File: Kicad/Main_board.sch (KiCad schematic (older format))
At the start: 138 parts, among them J1 Data, J2 Power, J3 Data, SW1 SW_Push, SW10 SW_Push, SW11 SW_Push, SW12 SW_Push, SW13 SW_Push, SW14 SW_Push, SW15 SW_Push, SW16 SW_Push, SW17 SW_Push, SW18 SW_Push, SW19 SW_Push, SW2 SW_Push, SW20 SW_Push, SW21 Rotary_Encoder_Switch, SW22 Rotary_Encoder_Switch, SW23 Rotary_Encoder_Switch, SW24 SW_Rotary8, SW3 SW_Push, SW4 SW_Push, SW5 SW_Push, SW6 SW_Push, SW7 SW_Push, SW8 SW_Push, SW9 SW_Push, U1 74HC595, U2 74HC595, U3 74HC595, U4 74HC595, U5 7_segment_3_digit_2831AS

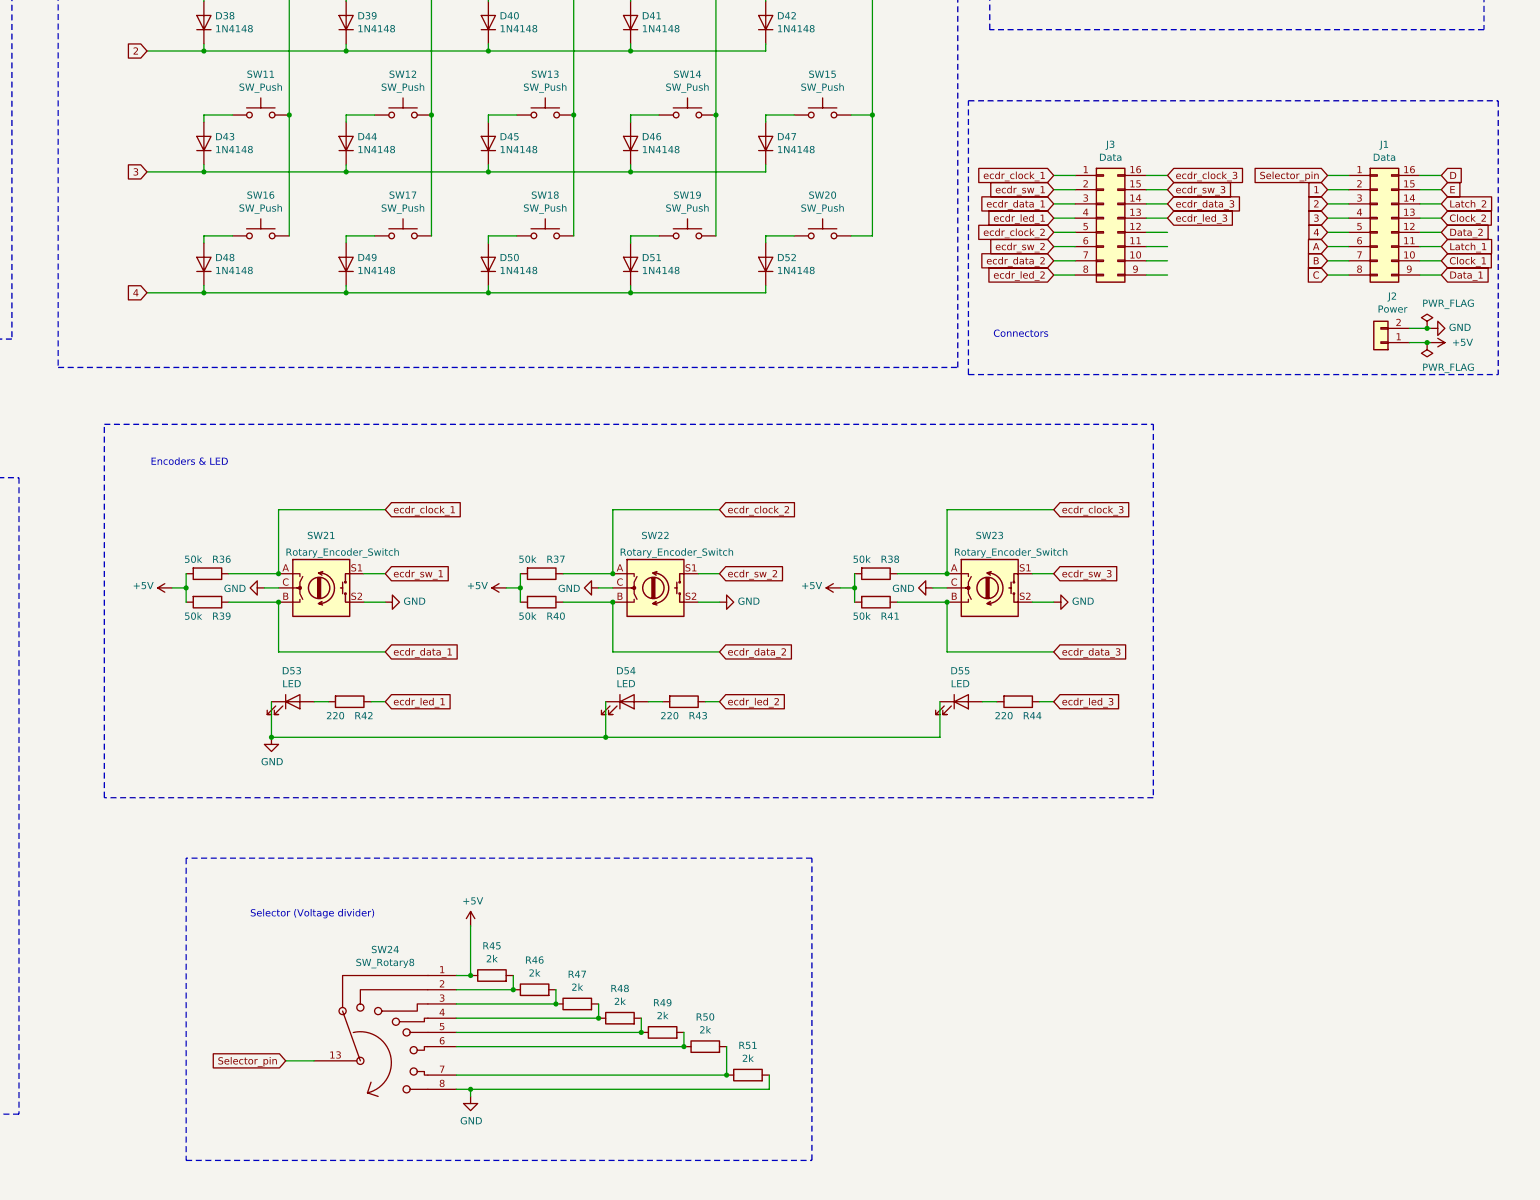
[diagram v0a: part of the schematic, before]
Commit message: modifié :         Kicad/Main_board-cache.lib 	modifié :         Kicad/Main_board.kicad_pcb 	modifié :         Kicad/Main_board.net 	modifié :         Kicad/Main_board.sch 	nouveau fichier : Kicad/My_library/00_Mes_empreintes.pretty/7-Segment_2831AS.kicad_mod 	modifié :         Kicad/My_library/00_Mes_empreintes.pretty/DIP-16_Socket.kicad_mod 	nouveau fichier : Kicad/My_library/00_Mes_empreintes.pretty/IDC-Header_2x04.kicad_mod 	nouveau fichier : Kicad/My_library/00_Mes_empreintes.pretty/IDC-Header_2x05.kicad_mod 	modifié :         Kicad/My_library/00_Mes_empreintes.pretty/IDC-Header_2x08.kicad_mod 	modifié :         Kicad/My_library/00_Mes_empreintes.pretty/LED_5.0mm.kicad_mod 	nouveau fichier : Kicad/My_library/00_Mes_empreintes.pretty/RotaryEncoder.kicad_mod 	modifié :         Kicad/My_library/00_Mes_empreintes.pretty/SW_PUSH-12mm(deported).kicad_mod 	modifié :         Kicad/My_library/00_Mes_symboles.bck 	modifié :         Kicad/My_library/00_Mes_symboles.dcm 	modifié :         Kicad/My_library/00_Mes_symboles.lib 	nouveau fichier : Kicad/My_library/Encoders.lib 	nouveau fichier : "Kicad/My_library/Mes_mod\303\250les_3D/216-resistors-in-tht-series-e24-from-1ohm-to-910mohm-1.snapshot.3/Yageo CFR-25 Resistor Axial P7.62mm 1,0 MOhm.stp" 	nouveau fichier : "Kicad/My_library/Mes_mod\303\250les_3D/216-resistors-in-tht-series-e24-from-1ohm-to-910mohm-1.snapshot.3/Yageo CFR-25 Resistor Axial P7.62mm 1,0 Ohm.stp" 	nouveau fichier : "Kicad/My_library/Mes_mod\303\250les_3D/216-resistors-in-tht-series-e24-from-1ohm-to-910mohm-1.snapshot.3/Yageo CFR-25 Resistor Axial P7.62mm 1,0 kOhm.stp" 	nouveau fichier : "Kicad/My_library/Mes_mod\303\250les_3D/216-resistors-in-tht-series-e24-from-1ohm-to-910mohm-1.snapshot.3/Yageo CFR-25 Resistor Axial P7.62mm 1,1 MOhm.stp" 	nouveau fichier : "Kicad/My_library/Mes_mod\303\250les_3D/216-resistors-in-tht-series-e24-from-1ohm-to-910mohm-1.snapshot.3/Yageo CFR-25 Resistor Axial P7.62mm 1,1 Ohm.stp" 	nouveau fichier : "Kicad/My_library/Mes_mod\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
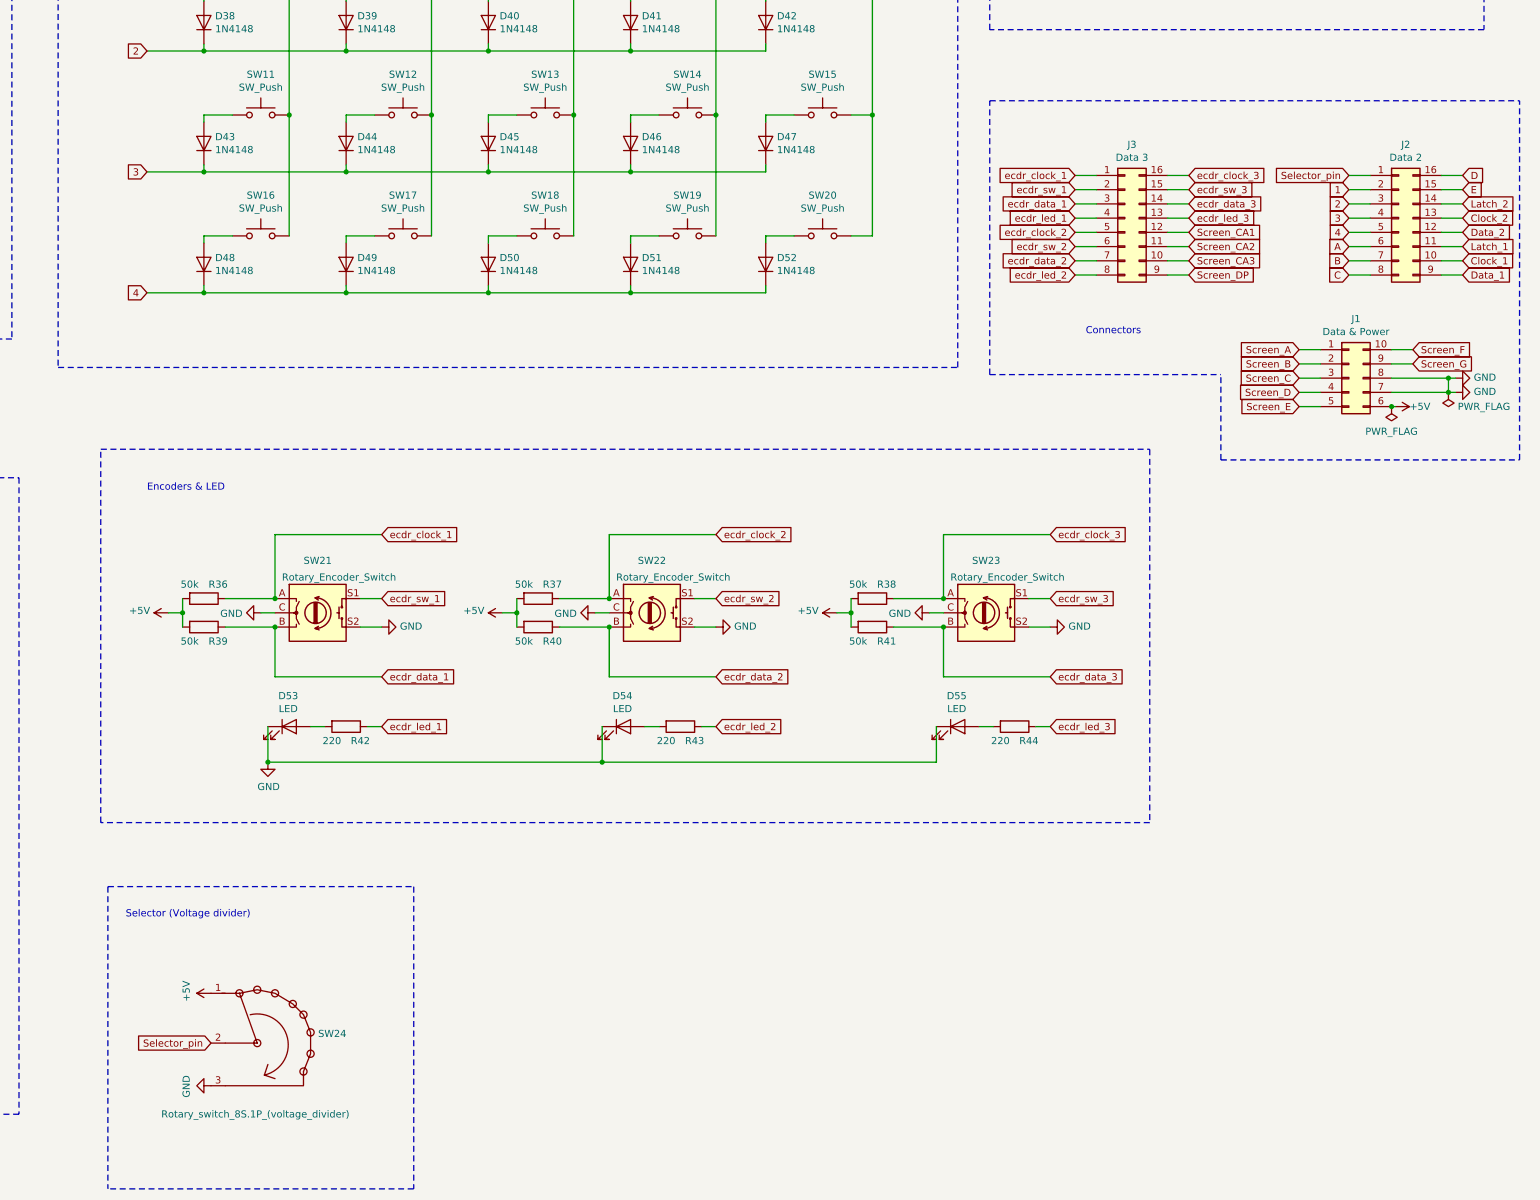
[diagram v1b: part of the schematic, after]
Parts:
- removed J2: Power, 00_Mes_empreintes:SolderWirePad_1x02_Drill1.5mm, symbol Connector_Generic:Conn_01x02
- removed R45, R46, R47, R48, R49, R50, R51: 2k, 00_Mes_empreintes:Resistance, symbol Device:R
- removed SW24: SW_Rotary8, symbol 00_Mes_symboles:SW_Rotary8-SW_Rotary_8
- added J1: Data & Power, 00_Mes_empreintes:IDC-Header_2x05, symbol Connector_Generic:Conn_02x05_Counter_Clockwise
- added SW24: Rotary_switch_8S.1P_(voltage_divider), 00_Mes_empreintes:SolderWirePad_1x03_Drill1.5mm, symbol 00_Mes_symboles:Rotary_switch_8S.1P_(voltage_divider)
- J2: renamed from J1; value Data -> Data 2
- J3: value Data -> Data 3
- SW21, SW22, SW23: footprint (none) -> 00_Mes_empreintes:RotaryEncoder
- U5: footprint (none) -> 00_Mes_empreintes:7-Segment_2831AS
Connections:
- net +5V: now also J1.6 (Pin_6), SW24.1
- net GND: now also J1.7 (Pin_7), J1.8 (Pin_8), SW24.3
- net Screen_A: now also J1.1 (Pin_1)
- net Screen_B: now also J1.2 (Pin_2)
- net Screen_C: now also J1.3 (Pin_3)
- net Screen_CA1: now also J3.12 (Pin_12)
- net Screen_CA2: now also J3.11 (Pin_11)
- net Screen_CA3: now also J3.10 (Pin_10)
- net Screen_D: now also J1.4 (Pin_4)
- net Screen_DP: now also J3.9 (Pin_9)
- net Screen_E: now also J1.5 (Pin_5)
- net Screen_F: now also J1.10 (Pin_10)
- net Screen_G: now also J1.9 (Pin_9)
- net Selector_pin: now also SW24.2
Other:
- moved on the sheet: D53, D54, D55, J2, J3, R36, R37, R38, R39, R40, R41, R42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
